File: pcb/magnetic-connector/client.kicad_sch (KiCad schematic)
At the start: 8 parts

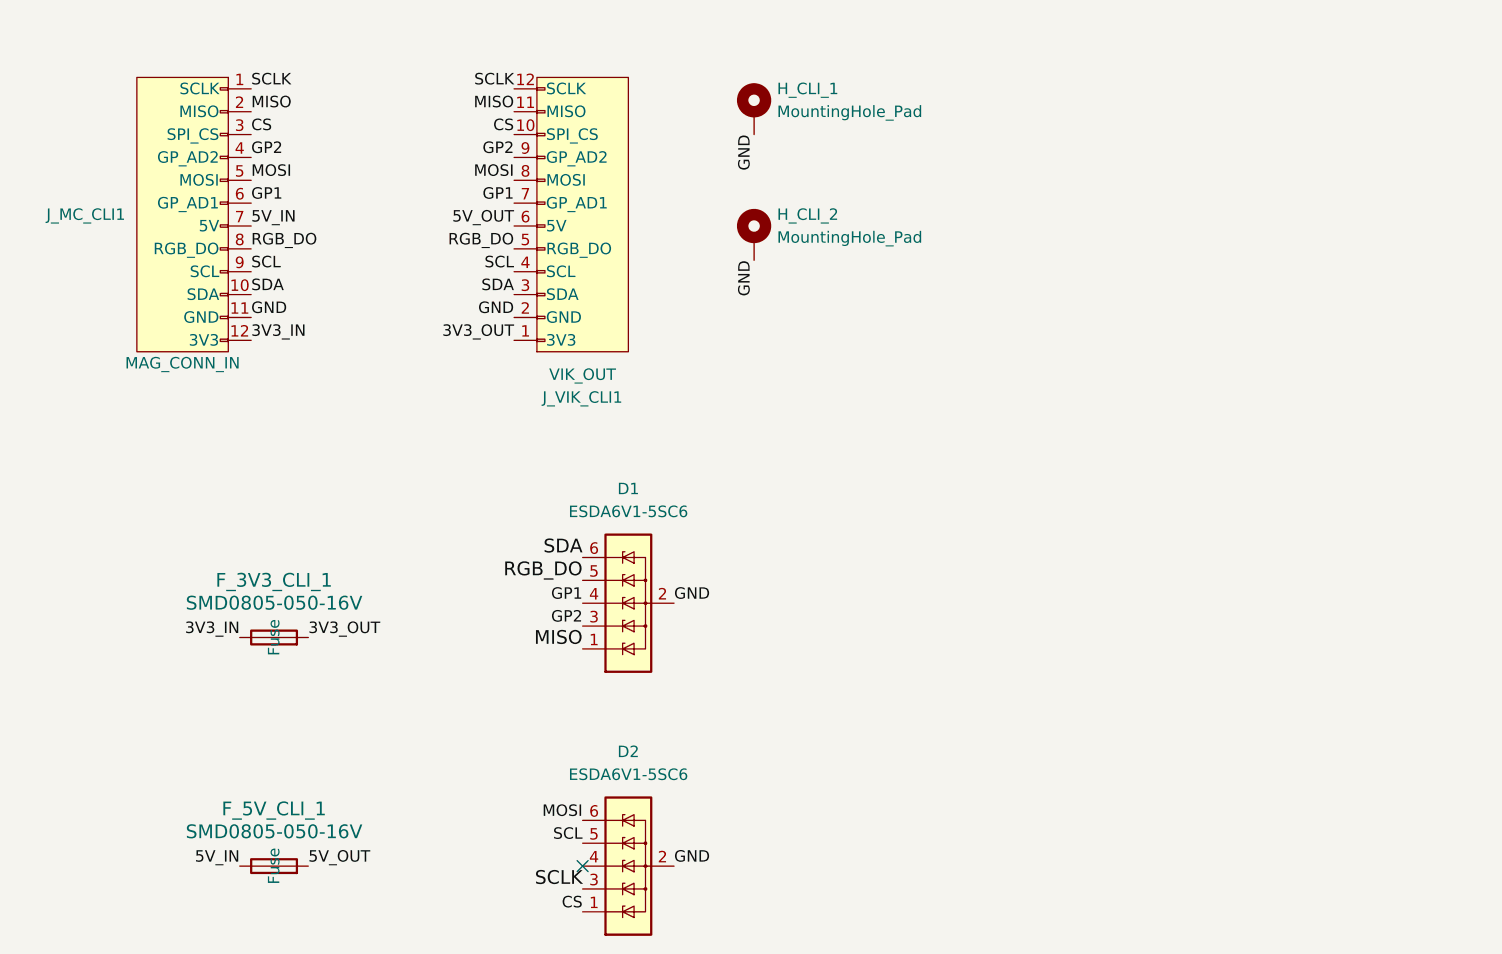
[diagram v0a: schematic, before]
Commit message: Change ESD protection chips on magnetic connector.
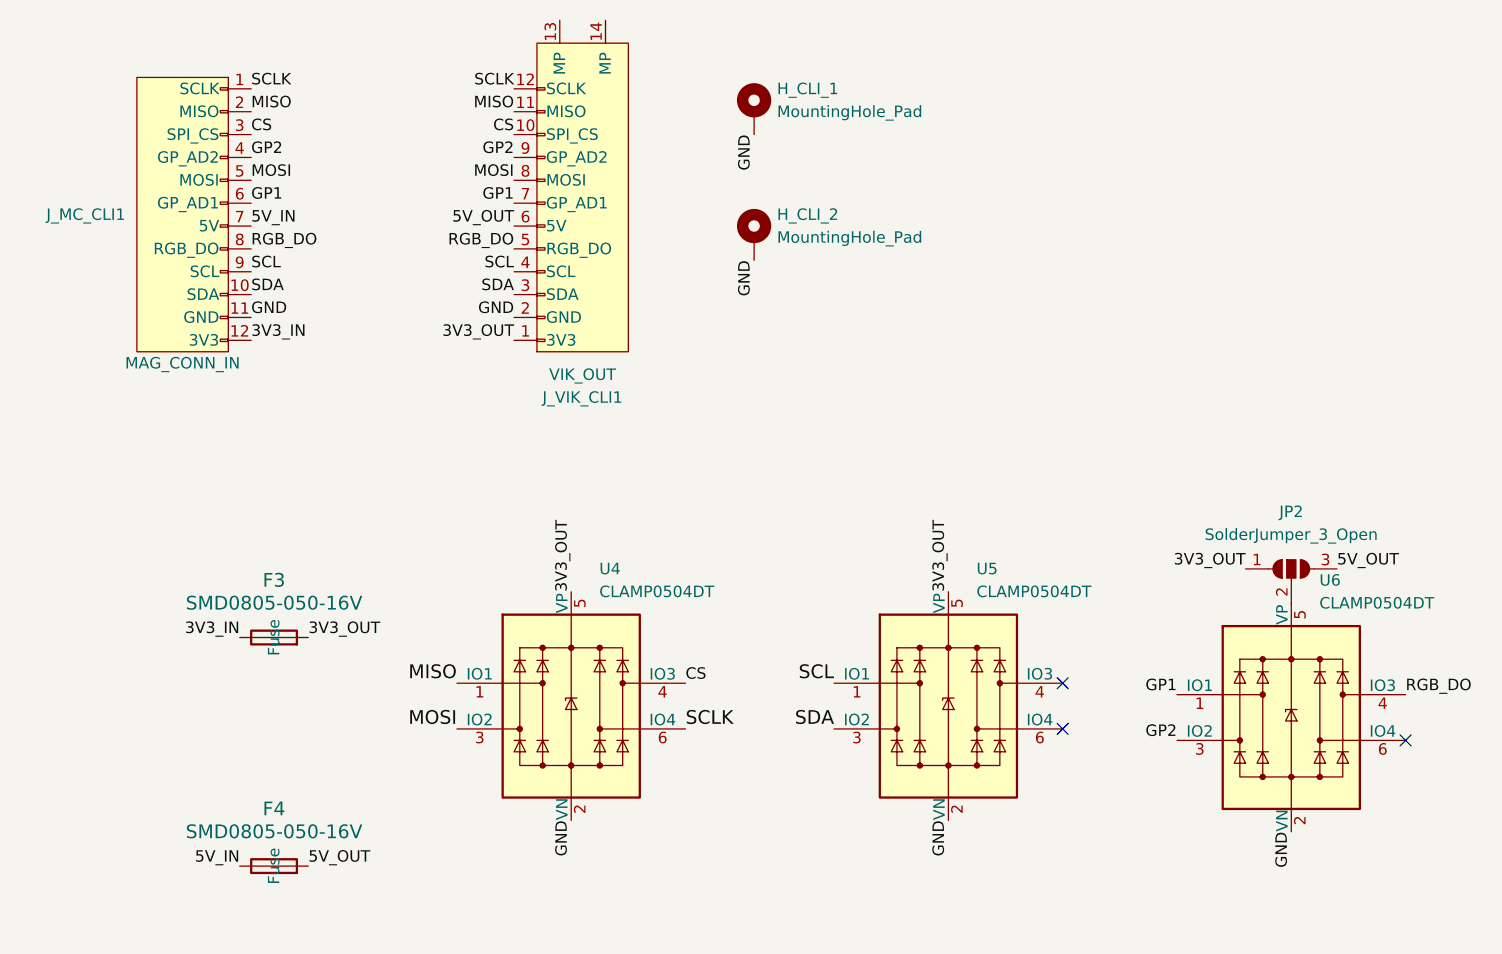
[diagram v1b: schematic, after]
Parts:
- removed D1, D2: ESDA6V1-5SC6, Package_TO_SOT_SMD:SOT-23-6, symbol Power_Protection:ESDA6V1-5SC6
- added JP2: SolderJumper_3_Open, Jumper:SolderJumper-3_P2.0mm_Open_TrianglePad1.0x1.5mm_NumberLabels, symbol Jumper:SolderJumper_3_Open
- added U4, U5, U6: CLAMP0504DT, Package_TO_SOT_SMD:SOT-23-6, symbol Power_Protection:SRV05-4
- J_VIK_CLI1: LCSC (none) -> C2856799
- renumbered F_3V3_CLI_1 to F3, F_5V_CLI_1 to F4
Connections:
- net 3V3_OUT: now also JP2.1 (A), U4.5 (VP), U5.5 (VP)
- net 5V_OUT: now also JP2.3 (B)
- net CS: now also U4.4 (IO3)
- net GND: now also U4.2 (VN), U5.2 (VN), U6.2 (VN)
- net GP1: now also U6.1 (IO1)
- net GP2: now also U6.3 (IO2)
- net MISO: now also U4.1 (IO1)
- net MOSI: now also U4.3 (IO2)
- net RGB_DO: now also U6.4 (IO3)
- net SCL: now also U5.1 (IO1)
- net SCLK: now also U4.6 (IO4)
- net SDA: now also U5.3 (IO2)
- new net: JP2.2 (C), U6.5 (VP)
- no-connect marks 1 -> 3
